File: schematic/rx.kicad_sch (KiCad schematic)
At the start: 34 parts, among them Q12 2N3904, U11 ADE-6

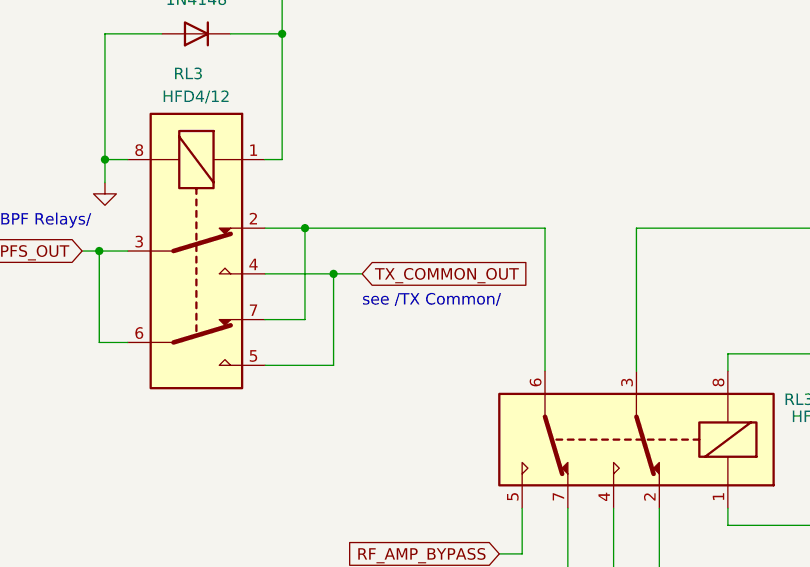
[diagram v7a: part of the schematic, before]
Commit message: Schematic: minor changes
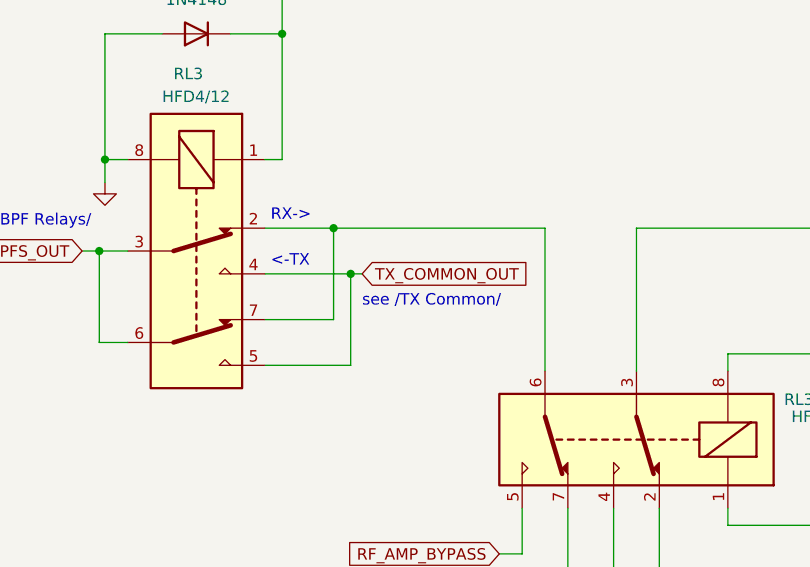
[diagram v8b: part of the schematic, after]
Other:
- note added: "<-TX"
- note added: "RX->"
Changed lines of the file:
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@@
   (junction (at 53.34 67.945) (diameter 0) (color 0 0 0 0)
   )
-  (junction (at 76.2 65.405) (diameter 0) (color 0 0 0 0)
+  (junction (at 81.28 70.485) (diameter 0) (color 0 0 0 0)
+  )
+  (junction (at 79.375 65.405) (diameter 0) (color 0 0 0 0)
   )
   (junction (at 203.835 41.91) (diameter 0) (color 0 0 0 0)
@@
   (junction (at 53.975 57.785) (diameter 0) (color 0 0 0 0)
   )
-  (junction (at 79.375 70.485) (diameter 0) (color 0 0 0 0)
-  )
   (junction (at 224.155 45.72) (diameter 0) (color 0 0 0 0)
   )
@@
     (stroke (width 0) (type default))
   )
-  (wire (pts (xy 79.375 80.645) (xy 79.375 70.485))
+  (wire (pts (xy 81.28 80.645) (xy 81.28 70.485))
+    (stroke (width 0) (type default))
+  )
+  (wire (pts (xy 81.28 70.485) (xy 82.55 70.485))
     (stroke (width 0) (type default))
   )
@@
     (stroke (width 0) (type default))
   )
-  (wire (pts (xy 76.2 75.565) (xy 71.755 75.565))
+  (wire (pts (xy 79.375 75.565) (xy 71.755 75.565))
     (stroke (width 0) (type default))
   )
@@
     (stroke (width 0) (type default))
   )
-  (wire (pts (xy 71.755 80.645) (xy 79.375 80.645))
+  (wire (pts (xy 71.755 80.645) (xy 81.28 80.645))
     (stroke (width 0) (type default))
   )
@@
     (stroke (width 0) (type default))
   )
-  (wire (pts (xy 71.755 65.405) (xy 76.2 65.405))
-    (stroke (width 0) (type default))
-  )
   (wire (pts (xy 110.49 169.545) (xy 121.285 169.545))
     (stroke (width 0) (type default))
@@
     (stroke (width 0) (type default))
   )
-  (wire (pts (xy 76.2 65.405) (xy 102.87 65.405))
+  (wire (pts (xy 71.755 65.405) (xy 79.375 65.405))
     (stroke (width 0) (type default))
   )
@@
     (stroke (width 0) (type default))
   )
-  (wire (pts (xy 71.755 70.485) (xy 79.375 70.485))
+  (wire (pts (xy 71.755 70.485) (xy 81.28 70.485))
     (stroke (width 0) (type default))
   )
@@
     (stroke (width 0) (type default))
   )
-  (wire (pts (xy 76.2 65.405) (xy 76.2 75.565))
+  (wire (pts (xy 79.375 65.405) (xy 79.375 75.565))
     (stroke (width 0) (type default))
   )
@@
     (stroke (width 0) (type default))
   )
+  (wire (pts (xy 79.375 65.405) (xy 102.87 65.405))
+    (stroke (width 0) (type default))
+  )
   (wire (pts (xy 227.965 31.75) (xy 227.965 34.29))
     (stroke (width 0) (type default))
@@
     (stroke (width 0) (type default))
   )
-  (wire (pts (xy 79.375 70.485) (xy 82.55 70.485))
-    (stroke (width 0) (type default))
-  )
   (wire (pts (xy 100.33 158.75) (xy 100.33 162.56))
     (stroke (width 0) (type default))
@@
     (effects (font (size 1.27 1.27)) (justify left bottom))
   )
+  (text "RX->" (at 72.39 64.77 0)
+    (effects (font (size 1.27 1.27)) (justify left bottom))
+  )
   (text "see /Root/" (at 141.605 102.235 0)
     (effects (font (size 1.27 1.27)) (justify left bottom))
@@
     (effects (font (size 1.27 1.27)) (justify left bottom))
   )
+  (text "<-TX" (at 72.39 69.85 0)
+    (effects (font (size 1.27 1.27)) (justify left bottom))
+  )
